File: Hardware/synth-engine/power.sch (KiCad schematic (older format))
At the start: 21 parts

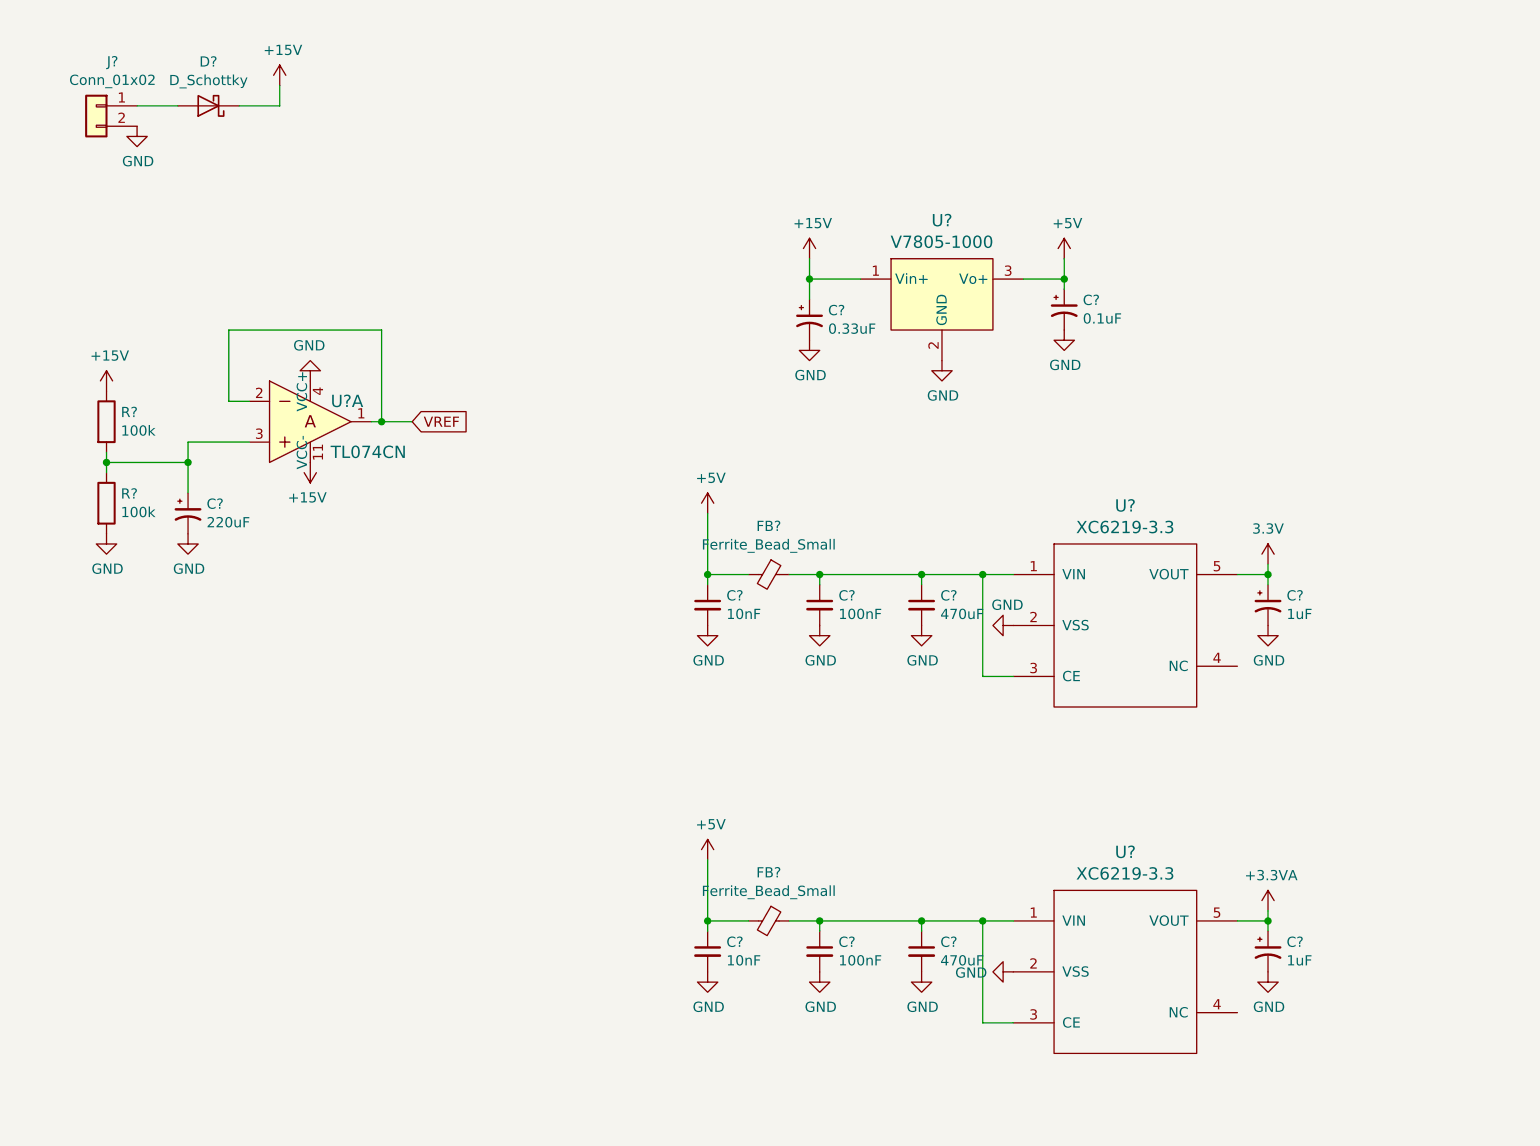
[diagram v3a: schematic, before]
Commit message: assign footprints to schematic symbols.
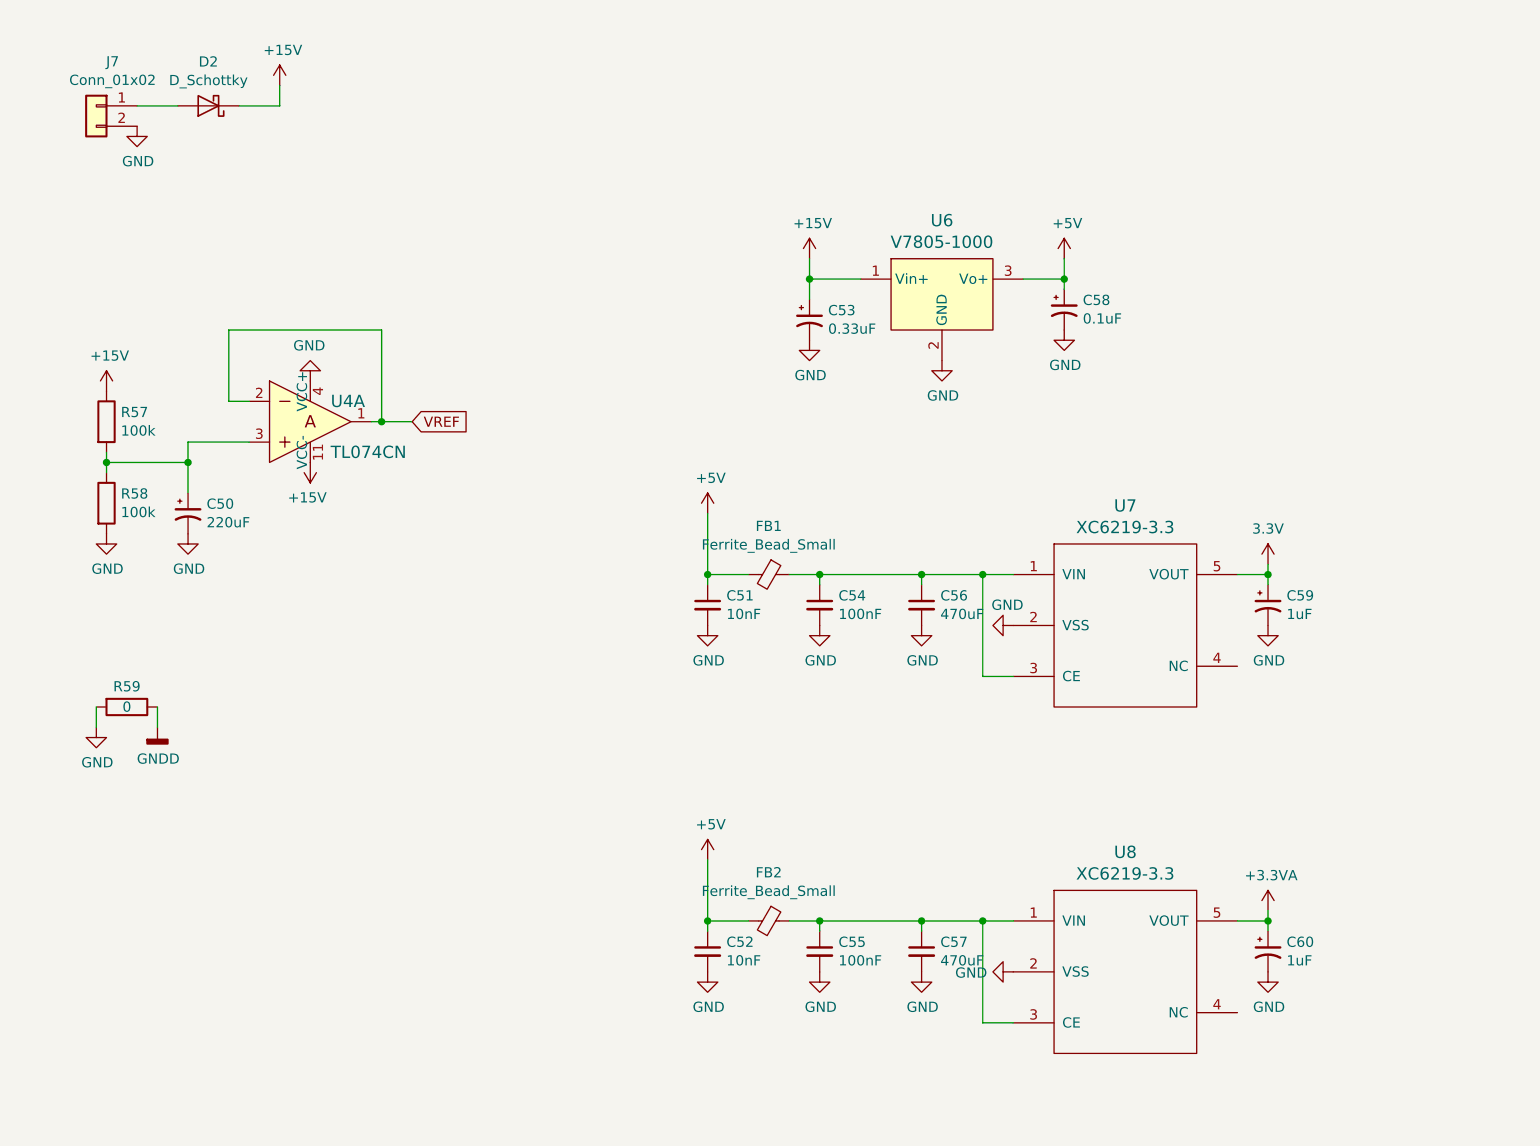
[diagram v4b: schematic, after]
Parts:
- added R59: 0, SparkFun-Passives:0805, symbol Device:R
- C50, C56, C57: renamed from C?; footprint (none) -> Capacitor_SMD:CP_Elec_6.3x5.4
- C51, C52, C53, C54, C55, C58, C59, C60: renamed from C?; footprint (none) -> SparkFun-Passives:0805
- D2: renamed from D?; footprint (none) -> SparkFun-DiscreteSemi:SMA-DIODE
- FB1, FB2: renamed from FB?; footprint (none) -> SparkFun-Passives:0805
- J7: renamed from J?; footprint (none) -> SparkFun-Connectors:1X02
- R57, R58: renamed from R?; footprint (none) -> SparkFun-Passives:0805
- U7, U8: renamed from U?; footprint (none) -> SparkFun-DigitalIC:SOT23-5
- gave numbers to parts that had none: 2
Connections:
- net GND: now also R59.2
- new net GNDD: R59.1

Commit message: rough placement and symbol organization. If I need to start PCB layout over from scracth, revert to this commit.
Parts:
- D2: footprint SparkFun-DiscreteSemi:SMA-DIODE -> SparkFun-DiscreteSemi:SMB-DIODE
- J7: footprint SparkFun-Connectors:1X02 -> SparkFun-Connectors:POWER_JACK_SLOT
- U4: footprint digikey-footprints:DIP-14_W3mm -> SparkFun-AnalogIC:SOIC8
- U6: footprint digikey-footprints:3-SIP_Module_V7805-1000 -> SparkFun-DiscreteSemi:DPAK
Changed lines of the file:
@@
 F 0 "J7" H 1320 1567 50  0000 C CNN
 F 1 "Conn_01x02" H 1320 1476 50  0000 C CNN
-F 2 "SparkFun-Connectors:1X02" H 1400 1350 50  0001 C CNN
+F 2 "SparkFun-Connectors:POWER_JACK_SLOT" H 1400 1350 50  0001 C CNN
 F 3 "~" H 1400 1350 50  0001 C CNN
 	1    1400 1350
@@
 F 0 "D2" H 1950 1134 50  0000 C CNN
 F 1 "D_Schottky" H 1950 1225 50  0000 C CNN
-F 2 "SparkFun-DiscreteSemi:SMA-DIODE" H 1950 1350 50  0001 C CNN
+F 2 "SparkFun-DiscreteSemi:SMB-DIODE" H 1950 1350 50  0001 C CNN
 F 3 "~" H 1950 1350 50  0001 C CNN
 	1    1950 1350
@@
 F 0 "U4" H 2550 3000 60  0000 L CNN
 F 1 "TL074CN" H 2550 2750 60  0000 L CNN
-F 2 "digikey-footprints:DIP-14_W3mm" H 2650 3100 60  0001 L CNN
+F 2 "SparkFun-AnalogIC:SOIC8" H 2650 3100 60  0001 L CNN
 F 3 "http://www.ti.com/lit/ds/symlink/tl071a.pdf" H 2650 3200 60  0001 L CNN
 F 4 "296-1777-5-ND" H 2650 3300 60  0001 L CNN "Digi-Key_PN"
@@
 F 0 "U6" H 5550 2687 60  0000 C CNN
 F 1 "V7805-1000" H 5550 2581 60  0000 C CNN
-F 2 "digikey-footprints:3-SIP_Module_V7805-1000" H 5750 2500 60  0001 L CNN
+F 2 "SparkFun-DiscreteSemi:DPAK" H 5750 2500 60  0001 L CNN
 F 3 "https://www.cui.com/product/resource/digikeypdf/v78xx-1000.pdf" H 5750 2600 60  0001 L CNN
 F 4 "102-1715-ND" H 5750 2700 60  0001 L CNN "Digi-Key_PN"

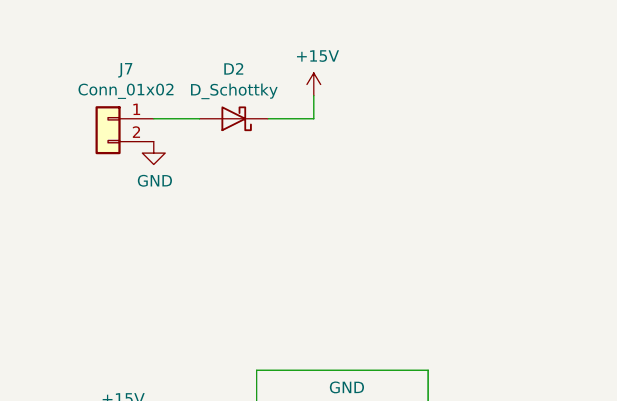
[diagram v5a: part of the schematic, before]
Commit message: add separate PCB with potentiometers and switches and connector between control board and synth engine
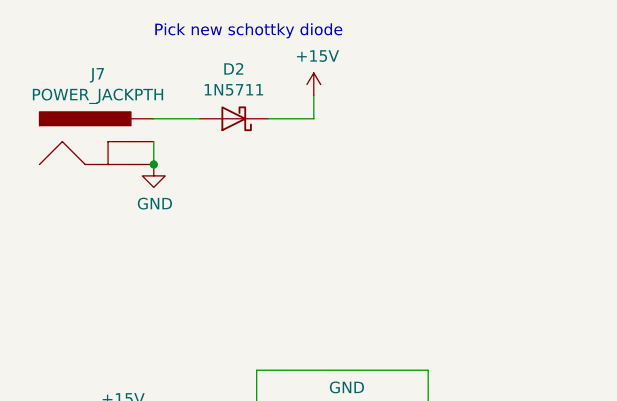
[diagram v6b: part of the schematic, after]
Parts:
- removed D2: D_Schottky, SparkFun-DiscreteSemi:SMB-DIODE, symbol Device:D_Schottky
- removed J7: Conn_01x02, SparkFun-Connectors:POWER_JACK_SLOT, symbol Connector_Generic:Conn_01x02
- added D2: 1N5711, SparkFun-Passives:1210, symbol Diode:1N5711
- added J7: POWER_JACKPTH, SparkFun-Connectors:POWER_JACK_PTH, symbol SparkFun-Connectors:POWER_JACKPTH
- U4: footprint SparkFun-AnalogIC:SOIC8 -> SparkFun-AnalogIC:SO16
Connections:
- net +15V: now also D2.1 (K)
- net GND: now also J7.GND, J7.GNDB (GNDBREAK)
- new net: D2.2 (A), J7.PWR
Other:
- note added: "Pick new schottky diode"
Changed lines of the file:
@@
 $Descr A4 11693 8268
 encoding utf-8
-Sheet 5 6
+Sheet 5 7
 Title ""
 Date ""
@@
 $EndDescr
 $Comp
-L Connector_Generic:Conn_01x02 J7
-U 1 1 5DD42AA9
-P 1400 1350
-F 0 "J7" H 1320 1567 50  0000 C CNN
-F 1 "Conn_01x02" H 1320 1476 50  0000 C CNN
-F 2 "SparkFun-Connectors:POWER_JACK_SLOT" H 1400 1350 50  0001 C CNN
-F 3 "~" H 1400 1350 50  0001 C CNN
-	1    1400 1350
-	-1   0    0    -1
-$EndComp
-$Comp
 L power:GND #PWR080
 U 1 1 5DD42D7D
-P 1600 1450
-F 0 "#PWR080" H 1600 1200 50  0001 C CNN
-F 1 "GND" H 1605 1277 50  0000 C CNN
-F 2 "" H 1600 1450 50  0001 C CNN
-F 3 "" H 1600 1450 50  0001 C CNN
-	1    1600 1450
-	1    0    0    -1
-$EndComp
-$Comp
-L Device:D_Schottky D2
-U 1 1 5DD42DBE
-P 1950 1350
-F 0 "D2" H 1950 1134 50  0000 C CNN
-F 1 "D_Schottky" H 1950 1225 50  0000 C CNN
-F 2 "SparkFun-DiscreteSemi:SMB-DIODE" H 1950 1350 50  0001 C CNN
-F 3 "~" H 1950 1350 50  0001 C CNN
-	1    1950 1350
-	-1   0    0    1
-$EndComp
-Wire Wire Line
-	1800 1350 1600 1350
+P 1600 1550
+F 0 "#PWR080" H 1600 1300 50  0001 C CNN
+F 1 "GND" H 1605 1377 50  0000 C CNN
+F 2 "" H 1600 1550 50  0001 C CNN
+F 3 "" H 1600 1550 50  0001 C CNN
+	1    1600 1550
+	1    0    0    -1
+$EndComp
 $Comp
 L power:+15V #PWR083
@@
 F 0 "U4" H 2550 3000 60  0000 L CNN
 F 1 "TL074CN" H 2550 2750 60  0000 L CNN
-F 2 "SparkFun-AnalogIC:SOIC8" H 2650 3100 60  0001 L CNN
+F 2 "SparkFun-AnalogIC:SO16" H 2650 3100 60  0001 L CNN
 F 3 "http://www.ti.com/lit/ds/symlink/tl071a.pdf" H 2650 3200 60  0001 L CNN
 F 4 "296-1777-5-ND" H 2650 3300 60  0001 L CNN "Digi-Key_PN"
@@
 Wire Wire Line
 	1700 4400 1700 4300
+$Comp
+L Diode:1N5711 D2
+U 1 1 5DDE1471
+P 1950 1350
+F 0 "D2" H 1950 1134 50  0000 C CNN
+F 1 "1N5711" H 1950 1225 50  0000 C CNN
+F 2 "SparkFun-Passives:1210" H 1950 1175 50  0001 C CNN
+F 3 "https://www.microsemi.com/document-portal/doc_download/8865-lds-0040-datasheet" H 1950 1350 50  0001 C CNN
+	1    1950 1350
+	-1   0    0    1
+$EndComp
+Text Notes 1600 1000 0    50   ~ 0
+Pick new schottky diode
+Wire Wire Line
+	1600 1350 1800 1350
+$Comp
+L SparkFun-Connectors:POWER_JACKPTH J7
+U 1 1 5DDEA308
+P 1500 1650
+F 0 "J7" H 1356 2145 50  0000 C CNN
+F 1 "POWER_JACKPTH" H 1356 2054 50  0000 C CNN
+F 2 "SparkFun-Connectors:POWER_JACK_PTH" H 1530 1800 20  0001 C CNN
+F 3 "" H 1500 1650 60  0000 C CNN
+	1    1500 1650
+	1    0    0    -1
+$EndComp
+Wire Wire Line
+	1600 1550 1600 1450
+Connection ~ 1600 1550
 $EndSCHEMATC

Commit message: fix some footprint errors
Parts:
- U6: footprint SparkFun-DiscreteSemi:DPAK -> SparkFun-DiscreteSemi:TO220V
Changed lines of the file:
@@
 F 0 "U6" H 5550 2687 60  0000 C CNN
 F 1 "V7805-1000" H 5550 2581 60  0000 C CNN
-F 2 "SparkFun-DiscreteSemi:DPAK" H 5750 2500 60  0001 L CNN
+F 2 "SparkFun-DiscreteSemi:TO220V" H 5750 2500 60  0001 L CNN
 F 3 "https://www.cui.com/product/resource/digikeypdf/v78xx-1000.pdf" H 5750 2600 60  0001 L CNN
 F 4 "102-1715-ND" H 5750 2700 60  0001 L CNN "Digi-Key_PN"
